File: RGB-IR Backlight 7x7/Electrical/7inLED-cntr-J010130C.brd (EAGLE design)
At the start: 144.7 x 25.4 mm, 54 parts, among them M1 TEENSY_3.1-3.2_DIL, P3 CON2X3, U1 LP2985-33DBVR, U2 AD5624R-3, U24 IL 710, U3 OPA4197IDR, U4 OPA4197IDR, U5 LMV344, U6 LMV344, U8 741G3157DBVR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

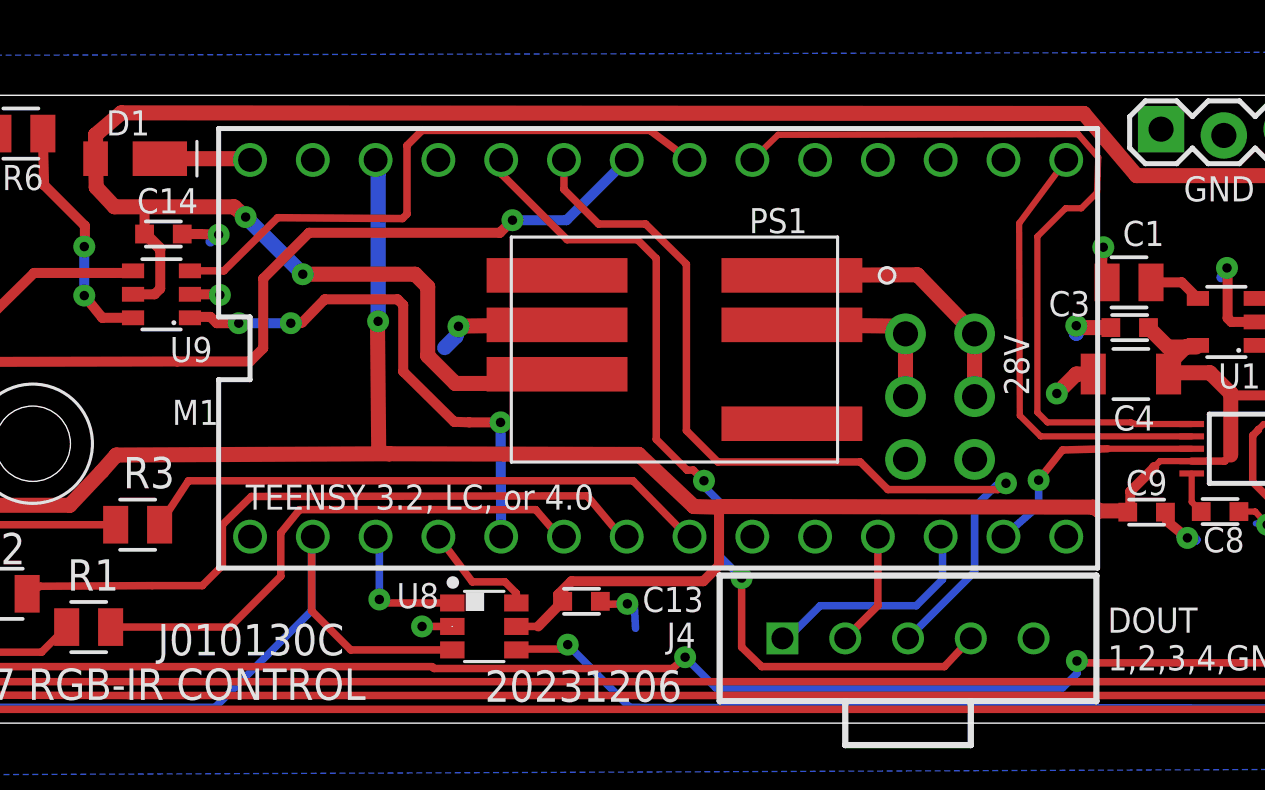
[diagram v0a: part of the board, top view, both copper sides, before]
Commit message: board change and FW update
Change Teensy connector to two parts so it can be put into Circuithub
Fix markerCmd - digital changes weren't changing pin state
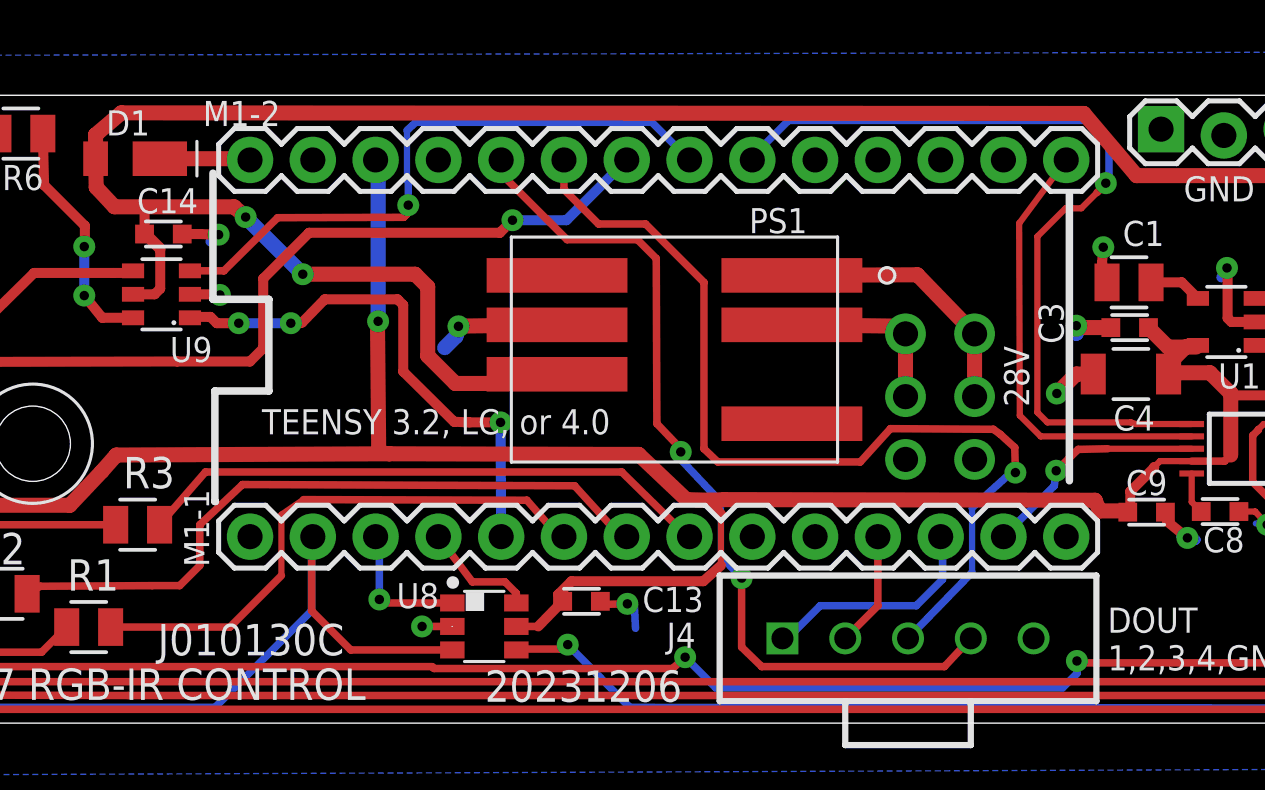
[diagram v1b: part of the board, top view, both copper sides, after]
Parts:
- removed M1: TEENSY_3.1-3.2_DIL, Teensy_3_and_LC_Series_Boards_v1.4:TEENSY_3.0-3.2&LC_DIL
- added M1-1, M1-2: (no value), SparkFun-Connectors:1X14
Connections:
- removed net MISO: M1.12
- removed net POSI: M1.11, U2.8
- new net CIPO: M1-1.14
- new net COPI: M1-1.13, U2.8
- net +3V3A: now also M1-2.3; no longer M1.3.3V
- net BLU: now also M1-1.8; no longer M1.6
- net DIR: now also M1-1.4; no longer M1.2
- net DOUT1: now also M1-1.12; no longer M1.10
- net DOUT2: now also M1-1.11; no longer M1.9
- net DOUT3: now also M1-2.6; no longer M1.21/A7
- net DOUT4: now also M1-2.5; no longer M1.22/A8
- net DOUTMARK: now also M1-2.4; no longer M1.23/A9
- net EN5: now also M1-1.9; no longer M1.7
- net EN6: now also M1-1.10; no longer M1.8
- net EN_1: now also M1-2.9; no longer M1.18/A4
- net GRN: now also M1-1.7; no longer M1.5
- net LED: now also M1-2.7; no longer M1.20/A6
- net LGND: now also M1-1.1, M1-2.2; no longer M1.AGND, M1.GND
- net LL: now also M1-2.12; no longer M1.15/A1
- net LR: now also M1-2.10; no longer M1.17/A3
- net OTMP: now also M1-2.13; no longer M1.14/A0
- net RED: now also M1-1.6; no longer M1.4
- net RX: now also M1-1.2; no longer M1.0
- net SCLK: now also M1-2.14; no longer M1.13
- net SYNCIN: now also M1-2.8; no longer M1.19/A5
- net TRIG: now also M1-1.5; no longer M1.3
- net TX: now also M1-1.3; no longer M1.1
- net UR: now also M1-2.11; no longer M1.16/A2
- net VIN: now also M1-2.1; no longer M1.VIN
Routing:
- net POSI: track 9.71 -> 0.00 mm, vias 1 -> 0
- net COPI: track 0.00 -> 9.36 mm, vias 0 -> 1
- net DOUT3: track 36.2 -> 38.4 mm
- net EN_1: track 32.9 -> 34.5 mm, vias 0 -> 1
- net SYNCIN: track 24.6 -> 25.3 mm, vias 0 -> 1
- net RED: track 22.2 -> 22.8 mm
- net +3V3A: track 205.0 -> 205.6 mm

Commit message: Update BOM and firmware
Comment out DEBUG define in FW
Update costing in BOM
Correct quantities, etc in BOM
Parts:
- U3, U4: value OPA4197IDR -> LMV344
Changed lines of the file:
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@@
 <attribute name="VALUE" x="-51.562" y="21.082" size="1.27" layer="28" rot="MR270"/>
 </element>
-<element name="U4" library="adafruit" package="SO14" value="OPA4197IDR" x="-42.037" y="7.366" smashed="yes" rot="R180">
+<element name="U4" library="adafruit" package="SO14" value="LMV344" x="-42.037" y="7.366" smashed="yes" rot="R180">
 <attribute name="VALUE" x="-38.481" y="8.001" size="1.27" layer="27" ratio="10" rot="R180"/>
 <attribute name="NAME" x="-37.4142" y="9.7536" size="1.016" layer="25" font="vector" ratio="10"/>
 </element>
-<element name="U3" library="adafruit" package="SO14" value="OPA4197IDR" x="-53.086" y="7.366" smashed="yes" rot="R180">
+<element name="U3" library="adafruit" package="SO14" value="LMV344" x="-53.086" y="7.366" smashed="yes" rot="R180">
 <attribute name="VALUE" x="-49.53" y="8.001" size="1.27" layer="27" ratio="10" rot="R180"/>
 <attribute name="NAME" x="-48.5648" y="9.652" size="1.016" layer="25" font="vector" ratio="10"/>
